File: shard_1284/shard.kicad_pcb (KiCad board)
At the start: 2 copper layers, 35 x 25 mm, 5 parts, among them J0 Shard, J1 ISP, U1 ATmega1284P-MU

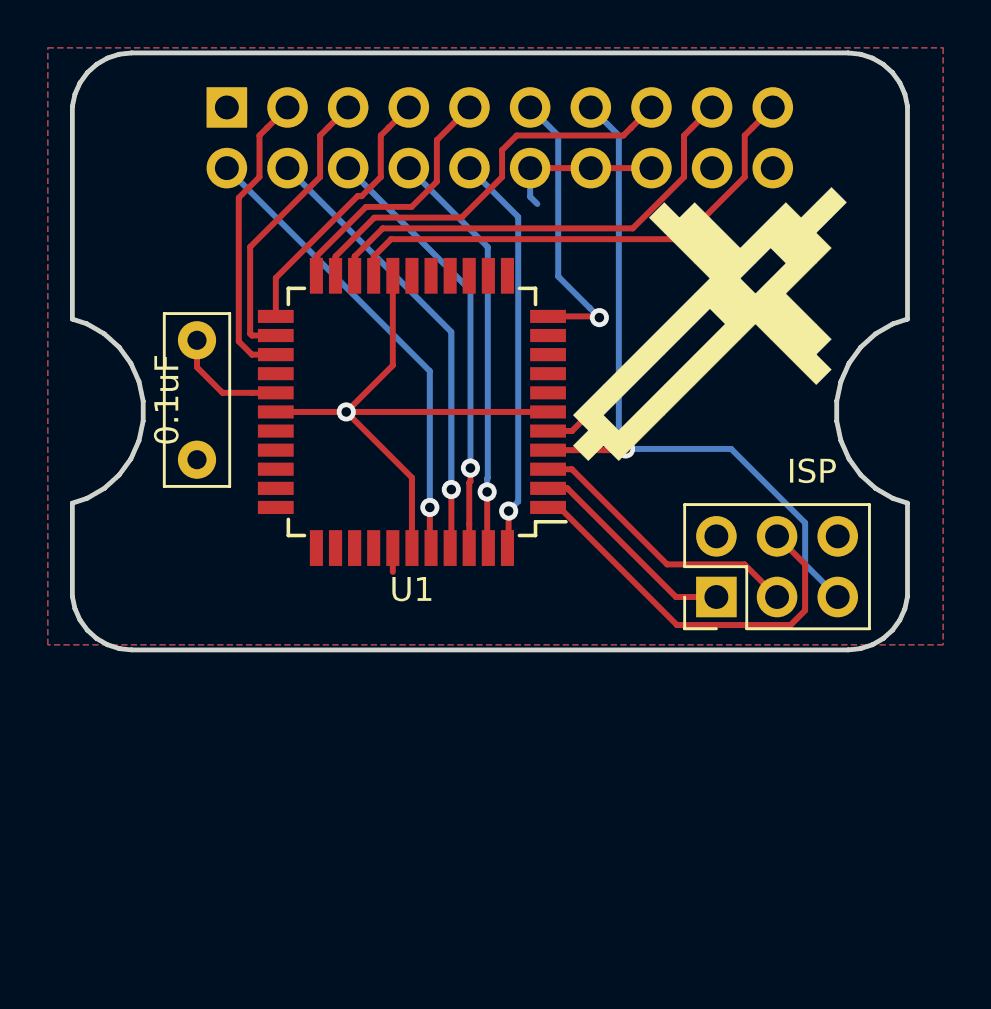
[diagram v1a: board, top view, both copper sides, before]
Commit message: flip connector
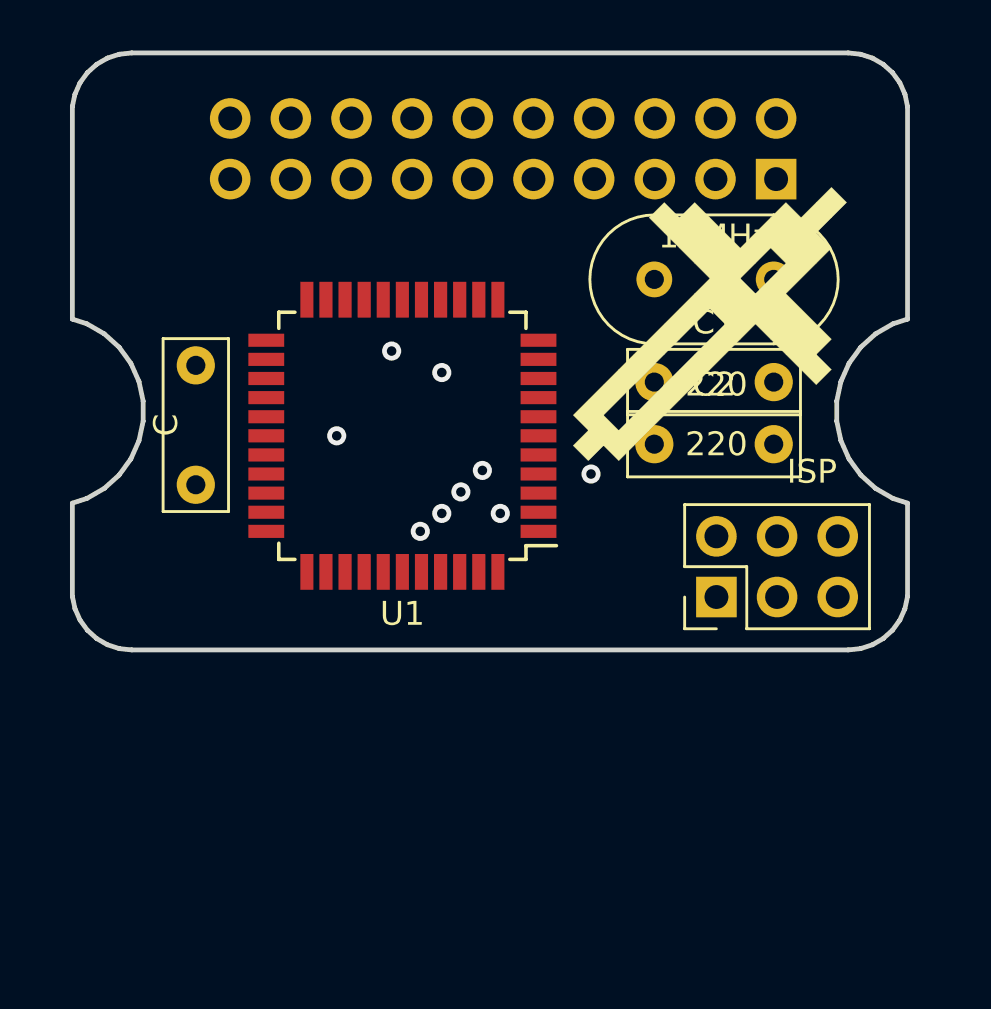
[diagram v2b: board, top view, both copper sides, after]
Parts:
- added C1: 220, Capacitor_THT:C_Rect_L7.0mm_W2.5mm_P5.00mm, F.Cu at (142.9, 66.5)
- added C2: 220, Capacitor_THT:C_Rect_L7.0mm_W2.5mm_P5.00mm, F.Cu at (142.9, 69.1)
- added Y1: 16MHz, Crystal:Resonator-2Pin_W10.0mm_H5.0mm, F.Cu at (147.9, 62.2)
- C0: value 0.1uF -> C
- moved J0 23.2 mm to (148.0, 58.0), turned to 90 degrees
- moved U1 1.08 mm to (132.3, 68.8)
- moved C0 1.05 mm to (123.7, 65.8)
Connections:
- J0 pad 10: D_SCK -> D_DC
- J0 pad 11: SND -> UP
- J0 pad 12: GND -> D_RST
- J0 pad 13: RESET -> RIGHT
- J0 pad 14: GND -> D_MOSI
- J0 pad 15: BTN_C -> LEFT
- J0 pad 16: GND -> D_SCK
- J0 pad 17: BTN_B -> DOWN
- J0 pad 18: GND -> SND
- J0 pad 19: BTN_A -> GND
- J0 pad 2: D_CS -> GND
- J0 pad 20: GND -> +3V3
- J0 pad 3: UP -> BTN_A
- J0 pad 4: D_DC -> D-
- J0 pad 5: DOWN -> BTN_B
- J0 pad 6: D_RST -> D+
- J0 pad 7: LEFT -> BTN_C
- J0 pad 8: D_MOSI -> D_CS
- J0 pad 9: RIGHT -> RESET
- U1 pad 10: Net-(U1-Pad10) -> D_MOSI
- U1 pad 11: SND -> Net-(U1-Pad11)
- U1 pad 14: Net-(U1-Pad14) -> SND
- U1 pad 22: RIGHT -> UP
- U1 pad 23: LEFT -> RIGHT
- U1 pad 24: DOWN -> LEFT
- U1 pad 25: UP -> DOWN
- U1 pad 40: D_CS -> D_SCK
- U1 pad 41: D_DC -> D_CS
- U1 pad 43: D_MOSI -> D_DC
- U1 pad 44: D_SCK -> Net-(U1-Pad44)
- U1 pad 9: Net-(U1-Pad9) -> D_MOSI
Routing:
- net GND: track 31.5 -> 0.00 mm
- net RESET: track 30.6 -> 0.00 mm
- net BTN_A: track 21.1 -> 0.00 mm
- net D_CS: track 19.5 -> 0.00 mm
- net BTN_B: track 19.4 -> 0.00 mm
- net D_DC: track 18.8 -> 0.00 mm
- net D_RST: track 18.1 -> 0.00 mm
- net D_MOSI: track 17.3 -> 0.00 mm
- net BTN_C: track 17.3 -> 0.00 mm
- net D_SCK: track 16.9 -> 0.00 mm
- net MOSI: track 16.6 -> 0.00 mm
- net UP: track 12.4 -> 0.00 mm
- net DOWN: track 12.3 -> 0.00 mm
- net SND: track 12.2 -> 0.00 mm
- net SCK: track 11.8 -> 0.00 mm
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- removed copper zone on F.Cu, net +3V3
- removed copper zone on B.Cu, net GND

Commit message: 1284 shard updated to edge connector
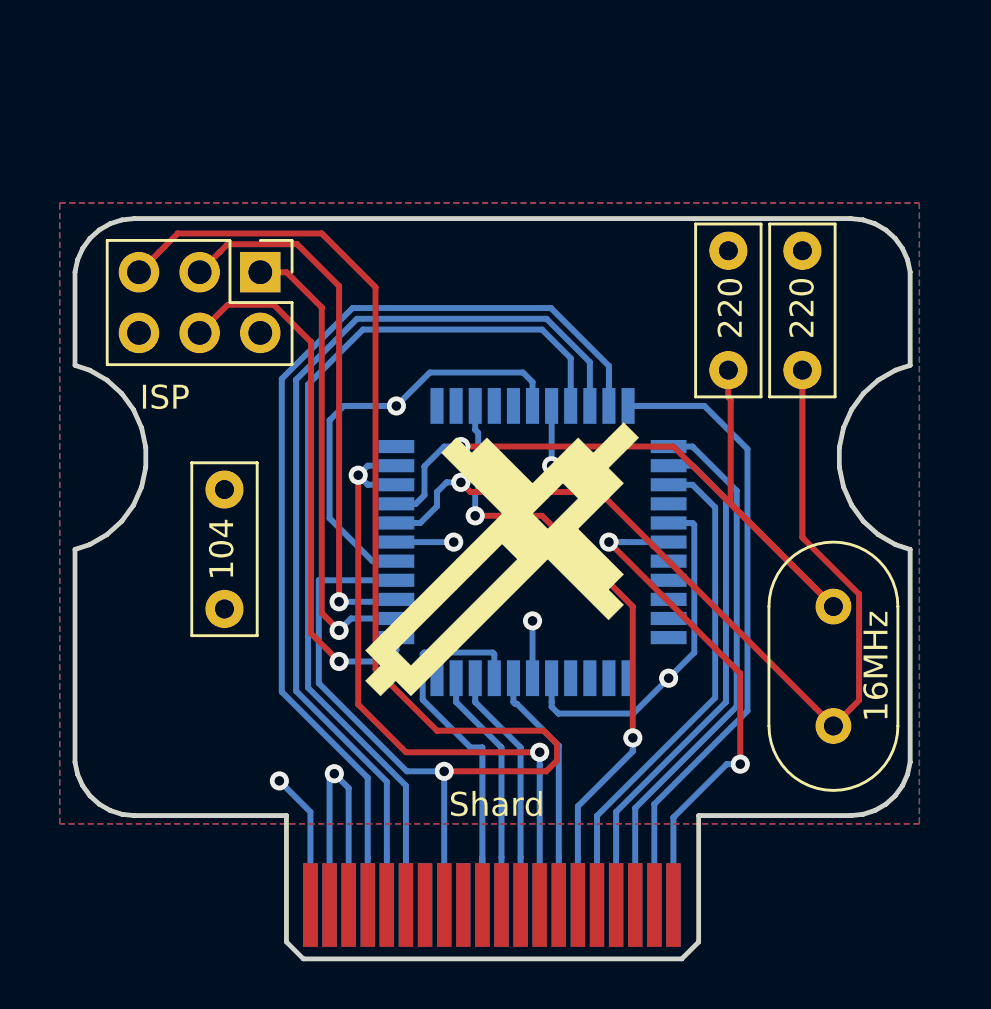
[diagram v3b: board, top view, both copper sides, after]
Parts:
- C0: value C -> 104
- J0: footprint Connector_PinHeader_2.54mm:PinHeader_2x10_P2.54mm_Vertical -> Custom Footprints:Samtec_MEC8-120-02-L-D-RA1_Edge; moved to F.Cu
- U1: moved to B.Cu
- moved J0 37.5 mm to (128.5, 90.0), turned to 0 degrees
- moved J1 23.4 mm to (126.4, 61.9), turned to 270 degrees
- moved Y1 18.9 mm to (150.4, 80.9), turned to 90 degrees
- moved SPIKE 13.1 mm to (137.8, 63.1)
- moved C0 10.3 mm to (124.9, 76.0), turned to 90 degrees
- moved U1 7.04 mm to (137.8, 73.2), turned to 0 degrees
- moved C2 6.93 mm to (149.1, 66.0), turned to 90 degrees
- moved C1 3.14 mm to (146.0, 66.0), turned to 90 degrees
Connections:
- J0 pad 1: +3V3 -> Net-(J0-Pad1)
- J0 pad 10: D_DC -> BTN_B
- J0 pad 11: UP -> Net-(J0-Pad11)
- J0 pad 12: D_RST -> BTN_C
- J0 pad 13: RIGHT -> Net-(J0-Pad13)
- J0 pad 14: D_MOSI -> Net-(J0-Pad14)
- J0 pad 15: LEFT -> Net-(J0-Pad15)
- J0 pad 16: D_SCK -> RESET
- J0 pad 17: DOWN -> Net-(J0-Pad17)
- J0 pad 18: SND -> Net-(J0-Pad18)
- J0 pad 19: GND -> Net-(J0-Pad19)
- J0 pad 2: GND -> +3V3
- J0 pad 20: +3V3 -> D_CS
- J0 pad 3: BTN_A -> Net-(J0-Pad3)
- J0 pad 4: D- -> GND
- J0 pad 5: BTN_B -> Net-(J0-Pad5)
- J0 pad 6: D+ -> GND
- J0 pad 7: BTN_C -> Net-(J0-Pad7)
- J0 pad 8: D_CS -> BTN_A
- J0 pad 9: RESET -> Net-(J0-Pad9)
- U1 pad 19: BTN_A -> BTN_C
- U1 pad 21: BTN_C -> BTN_A
- U1 pad 22: UP -> RIGHT
- U1 pad 23: RIGHT -> LEFT
- U1 pad 24: LEFT -> DOWN
- U1 pad 25: DOWN -> UP
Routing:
- net RESET: track 0.00 -> 62.0 mm
- net BTN_A: track 0.00 -> 41.1 mm
- net GND: track 0.00 -> 40.1 mm, vias 1 -> 6
- net Net-(C2-Pad1): track 0.00 -> 39.9 mm, vias 0 -> 1
- net BTN_B: track 0.00 -> 39.5 mm
- net +3V3: track 0.00 -> 38.7 mm, vias 0 -> 3
- net BTN_C: track 0.00 -> 37.9 mm
- net Net-(C1-Pad1): track 0.00 -> 34.5 mm, vias 0 -> 1
- net D_MOSI: track 0.00 -> 28.0 mm, vias 1 -> 2
- net RIGHT: track 0.00 -> 26.5 mm
- net SND: track 0.00 -> 26.3 mm, vias 1 -> 2
- net MOSI: track 0.00 -> 22.8 mm, vias 0 -> 1
- net LEFT: track 0.00 -> 22.7 mm
- net SCK: track 0.00 -> 22.7 mm, vias 0 -> 1
- net DOWN: track 0.00 -> 21.9 mm
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- added copper zone on F.Cu, net +3V3
- added copper zone on B.Cu, net GND
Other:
- board size 35 x 25 mm -> 35 x 31 mm

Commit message: tweaked labels
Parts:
- U1: value ATmega1284P-MU -> ATmega1284P
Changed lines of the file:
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@@
-(kicad_pcb (version 20171130) (host pcbnew "(5.0.1-3-g963ef8bb5)")
+(kicad_pcb (version 20171130) (host pcbnew "(5.0.0)")
   (general
     (thickness 1.6)
@@
     (solder_mask_min_width 0.25)
     (aux_axis_origin 0 0)
-    (visible_elements FFFFF77F)
+    (visible_elements 7FFFFFFF)
     (pcbplotparams
       (layerselection 0x010fc_ffffffff)
@@
       (drillshape 0)
       (scaleselection 1)
-      (outputdirectory "/Users/mikewatts/Desktop/shard1284_gerbers/"))
+      (outputdirectory "../../../Scratch/Spike_Gerbers/Shard_1284/"))
   )
   (net 0 "")
@@
       (effects (font (size 1 1) (thickness 0.15)) (justify mirror))
     )
-    (fp_text value ATmega1284P-MU (at 0 -7.45) (layer B.SilkS)
+    (fp_text value ATmega1284P (at 0 -7.45) (layer B.SilkS)
       (effects (font (size 1 1) (thickness 0.15)) (justify mirror))
     )
@@
   (gr_line (start 153 66) (end 153.61325 65.8008) (layer Edge.Cuts) (width 0.2))
   (gr_line (start 132.6 77.9) (end 136.6 73.9) (layer F.Mask) (width 1))
-  (via (at 142 81.4) (size 0.8) (drill 0.4) (layers F.Cu B.Cu) (net 11))
-  (via (at 134.8 70.7) (size 0.8) (drill 0.4) (layers F.Cu B.Cu) (net 35))
-  (via (at 134.8 69.2) (size 0.8) (drill 0.4) (layers F.Cu B.Cu) (net 34))
-  (via (at 129.7 78.2) (size 0.8) (drill 0.4) (layers F.Cu B.Cu) (net 18))
-  (via (at 129.7 76.9) (size 0.8) (drill 0.4) (layers F.Cu B.Cu) (net 16))
-  (via (at 129.7 75.7) (size 0.8) (drill 0.4) (layers F.Cu B.Cu) (net 17))
-  (via (at 141 73.2) (size 0.8) (drill 0.4) (layers F.Cu B.Cu) (net 25))
   (via (at 143.5 78.9) (size 0.8) (drill 0.4) (layers F.Cu B.Cu) (net 1))
   (via (at 132.1 67.5) (size 0.8) (drill 0.4) (layers F.Cu B.Cu) (net 1))
@@
   (segment (start 137.075001 79.975001) (end 137.148003 79.975001) (width 0.25) (layer B.Cu) (net 10))
   (segment (start 137 79.9) (end 137.075001 79.975001) (width 0.25) (layer B.Cu) (net 10))
+  (via (at 142 81.4) (size 0.8) (drill 0.4) (layers F.Cu B.Cu) (net 11))
   (via (at 135.4 72.1) (size 0.8) (drill 0.4) (layers F.Cu B.Cu) (net 11))
   (segment (start 138.2 72.1) (end 135.4 72.1) (width 0.25) (layer F.Cu) (net 11))
@@
   (segment (start 138.5728 63.39998) (end 130.263609 63.399981) (width 0.25) (layer B.Cu) (net 15))
   (segment (start 130.263609 63.399981) (end 127.3 66.36359) (width 0.25) (layer B.Cu) (net 15))
+  (via (at 129.7 76.9) (size 0.8) (drill 0.4) (layers F.Cu B.Cu) (net 16))
   (segment (start 130.2 76.4) (end 132.1 76.4) (width 0.25) (layer B.Cu) (net 16))
   (segment (start 129.7 76.9) (end 130.2 76.4) (width 0.25) (layer B.Cu) (net 16))
@@
   (segment (start 128.974999 76.174999) (end 128.974999 63.374999) (width 0.25) (layer F.Cu) (net 16))
   (segment (start 129.7 76.9) (end 128.974999 76.174999) (width 0.25) (layer F.Cu) (net 16))
+  (via (at 129.7 75.7) (size 0.8) (drill 0.4) (layers F.Cu B.Cu) (net 17))
   (segment (start 132 75.7) (end 132.1 75.6) (width 0.25) (layer B.Cu) (net 17))
   (segment (start 129.7 75.7) (end 132 75.7) (width 0.25) (layer B.Cu) (net 17))
@@
   (segment (start 129.7 62.47921) (end 127.945789 60.724999) (width 0.25) (layer F.Cu) (net 17))
   (segment (start 129.7 75.7) (end 129.7 62.47921) (width 0.25) (layer F.Cu) (net 17))
+  (via (at 129.7 78.2) (size 0.8) (drill 0.4) (layers F.Cu B.Cu) (net 18))
   (segment (start 132.1 77.725) (end 132.1 77.2) (width 0.25) (layer B.Cu) (net 18))
   (segment (start 131.625 78.2) (end 132.1 77.725) (width 0.25) (layer B.Cu) (net 18))
@@
   (segment (start 125.035001 63.264999) (end 124.709999 63.590001) (width 0.25) (layer F.Cu) (net 18))
   (segment (start 128.52499 77.02499) (end 128.52499 64.825988) (width 0.25) (layer F.Cu) (net 18))
+  (via (at 141 73.2) (size 0.8) (drill 0.4) (layers F.Cu B.Cu) (net 25))
   (via (at 138.6 70) (size 0.8) (drill 0.4) (layers F.Cu B.Cu) (net 25))
   (via (at 134.5 73.2) (size 0.8) (drill 0.4) (layers F.Cu B.Cu) (net 25))
@@
   (segment (start 130.1 83.5) (end 129.5 82.9) (width 0.25) (layer B.Cu) (net 25))
   (segment (start 130.1 88.4) (end 130.1 83.5) (width 0.25) (layer B.Cu) (net 25))
+  (via (at 134.8 69.2) (size 0.8) (drill 0.4) (layers F.Cu B.Cu) (net 34))
   (segment (start 133.274999 71.235003) (end 133.274999 70.025001) (width 0.25) (layer B.Cu) (net 34))
   (segment (start 132.910002 71.6) (end 133.274999 71.235003) (width 0.25) (layer B.Cu) (net 34))
@@
   (segment (start 146 67.13137) (end 146.1 67.23137) (width 0.25) (layer F.Cu) (net 34))
   (segment (start 146 66) (end 146 67.13137) (width 0.25) (layer F.Cu) (net 34))
+  (via (at 134.8 70.7) (size 0.8) (drill 0.4) (layers F.Cu B.Cu) (net 35))
   (segment (start 133.1 72.4) (end 133.8 71.7) (width 0.25) (layer B.Cu) (net 35))
   (segment (start 132.1 72.4) (end 133.1 72.4) (width 0.25) (layer B.Cu) (net 35))
